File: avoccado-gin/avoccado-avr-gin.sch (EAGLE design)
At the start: 55 parts, among them Q1 16MHz, Q2 FET, U1 MPU-6000QFN-24, U2 MCP73831

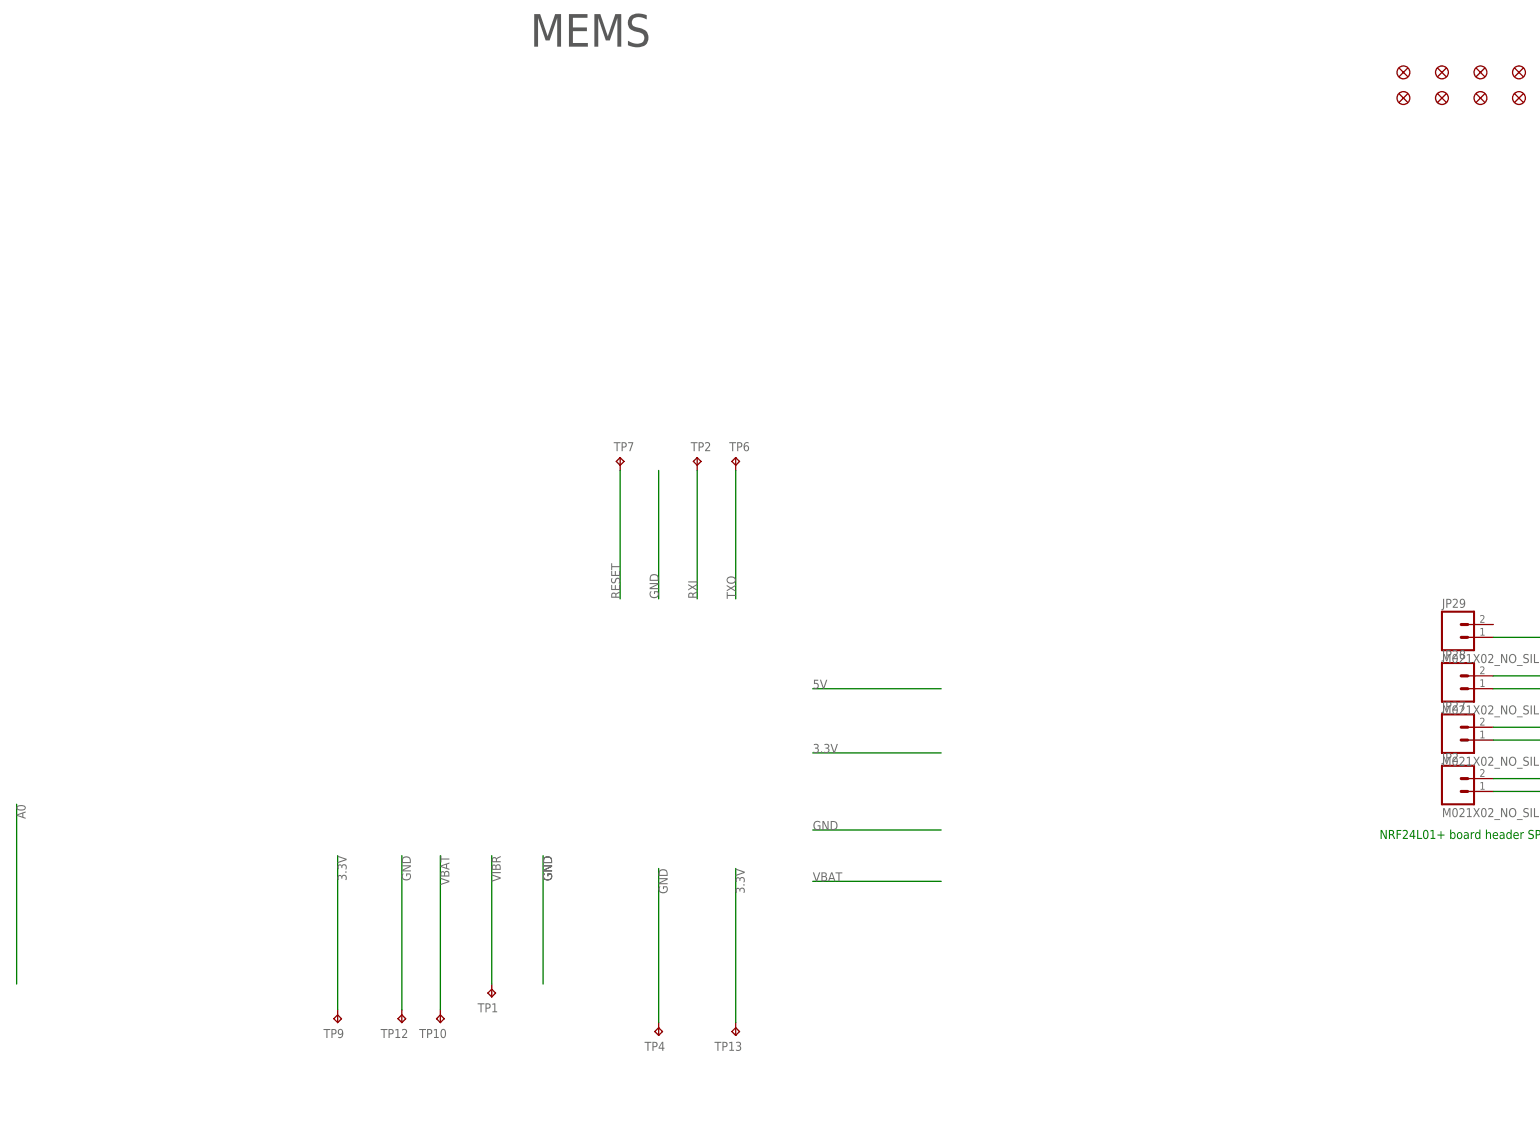
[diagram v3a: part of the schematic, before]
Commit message: add SMD pads to bottom layer
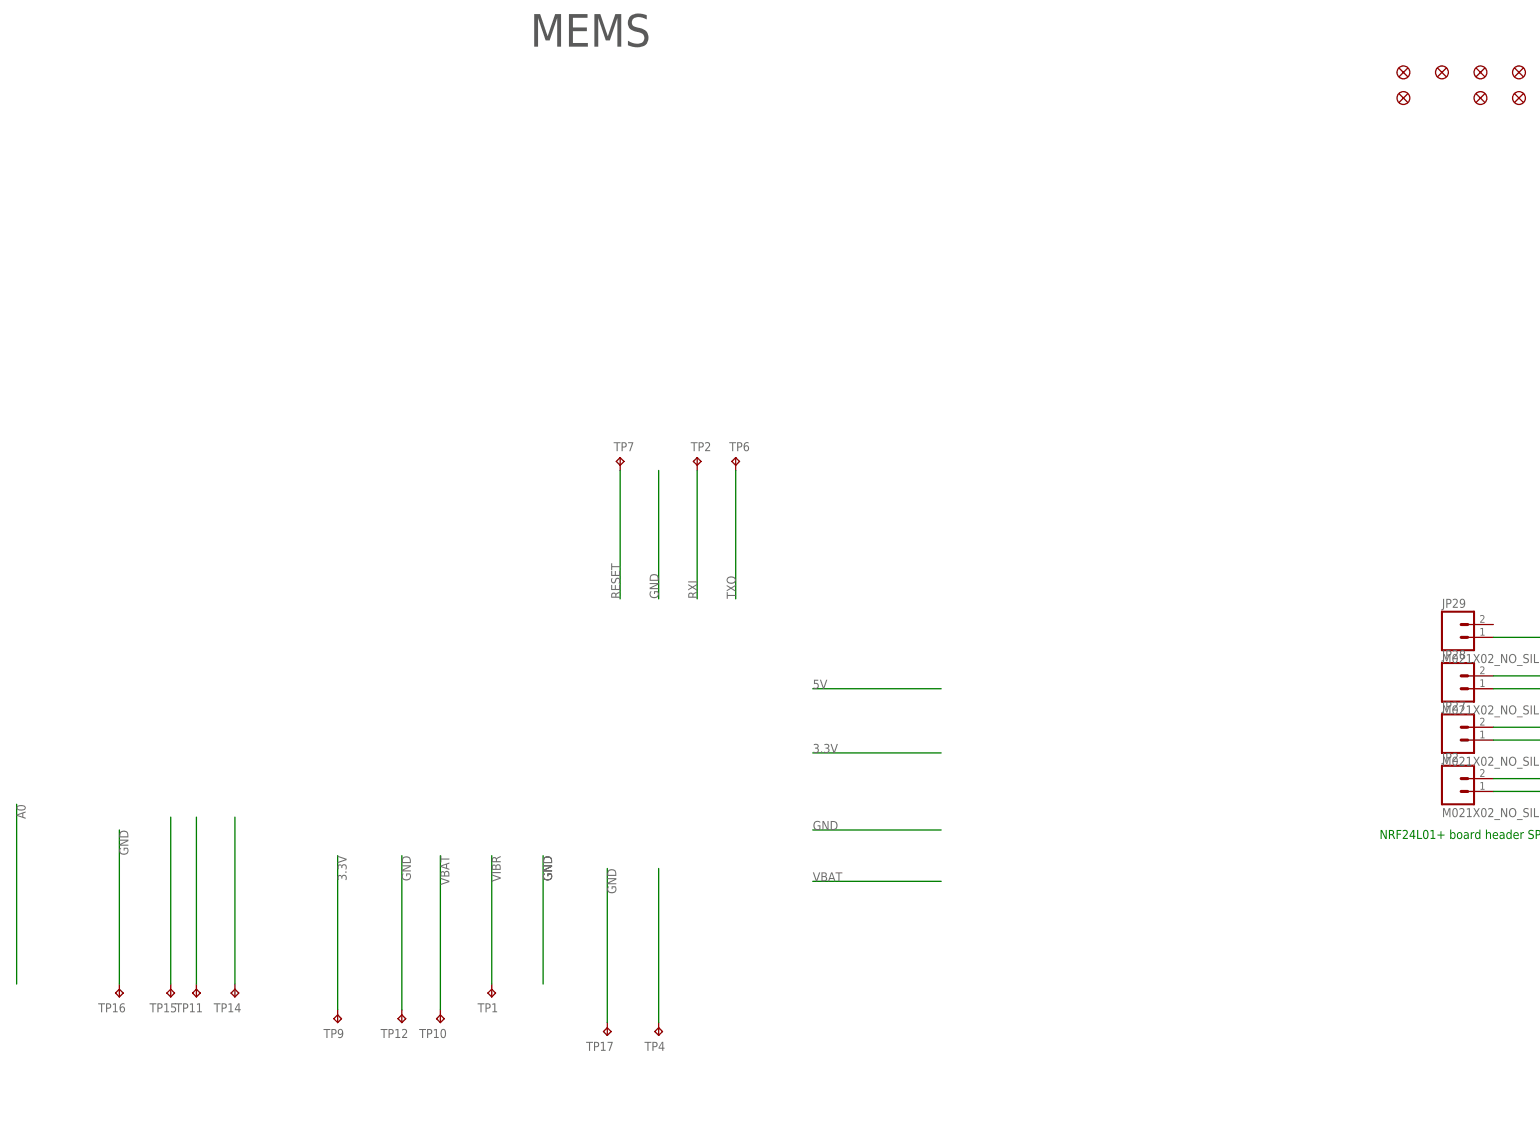
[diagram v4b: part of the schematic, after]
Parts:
- removed FID7: FIDUCIALUFIDUCIAL, SparkFun-Aesthetics:FIDUCIALUFIDUCIAL
- removed TP13: TPTP20R, testpad:TPTP20R
- added TP11, TP14, TP15, TP16, TP17: TPTP20R, testpad:TPTP20R
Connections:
- net 3.3V: no longer TP13.TP
- net D5: now also TP15.TP
- net D7: now also TP14.TP
- net D8: now also TP11.TP
- net GND: now also TP16.TP, TP17.TP; no longer TP4.TP
- net VBAT: now also TP4.TP
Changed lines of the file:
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@@
 <part name="TP10" library="testpad" deviceset="TP" device="TP20R"/>
 <part name="TP12" library="testpad" deviceset="TP" device="TP20R"/>
-<part name="TP13" library="testpad" deviceset="TP" device="TP20R"/>
 <part name="TP4" library="testpad" deviceset="TP" device="TP20R"/>
 <part name="FRAME2" library="frames" deviceset="LETTER_L" device=""/>
@@
 <part name="FID5" library="SparkFun-Aesthetics" deviceset="FIDUCIAL" device="UFIDUCIAL"/>
 <part name="FID6" library="SparkFun-Aesthetics" deviceset="FIDUCIAL" device="UFIDUCIAL"/>
-<part name="FID7" library="SparkFun-Aesthetics" deviceset="FIDUCIAL" device="UFIDUCIAL"/>
 <part name="FID8" library="SparkFun-Aesthetics" deviceset="FIDUCIAL" device="UFIDUCIAL"/>
 <part name="FID9" library="SparkFun-Aesthetics" deviceset="FIDUCIAL" device="UFIDUCIAL"/>
@@
 <part name="TP8" library="testpad" deviceset="TP" device="TP20R"/>
 <part name="TP9" library="testpad" deviceset="TP" device="TP20R"/>
+<part name="TP11" library="testpad" deviceset="TP" device="TP20R"/>
+<part name="TP14" library="testpad" deviceset="TP" device="TP20R"/>
+<part name="TP15" library="testpad" deviceset="TP" device="TP20R"/>
+<part name="TP16" library="testpad" deviceset="TP" device="TP20R"/>
+<part name="TP17" library="testpad" deviceset="TP" device="TP20R"/>
 </parts>
 <sheets>
@@
 <instance part="TP10" gate="G$1" x="421.64" y="58.42" rot="R180"/>
 <instance part="TP12" gate="G$1" x="414.02" y="58.42" rot="R180"/>
-<instance part="TP13" gate="G$1" x="480.06" y="55.88" rot="R180"/>
 <instance part="TP4" gate="G$1" x="464.82" y="55.88" rot="R180"/>
 <instance part="FRAME2" gate="G$1" x="0" y="226.06"/>
@@
 <instance part="FID5" gate="G$1" x="642.62" y="246.38"/>
 <instance part="FID6" gate="G$1" x="612.14" y="241.3"/>
-<instance part="FID7" gate="G$1" x="619.76" y="241.3"/>
 <instance part="FID8" gate="G$1" x="627.38" y="241.3"/>
 <instance part="FID9" gate="G$1" x="635" y="241.3"/>
@@
 <instance part="TP8" gate="G$1" x="330.2" y="63.5" rot="R180"/>
 <instance part="TP9" gate="G$1" x="401.32" y="58.42" rot="R180"/>
+<instance part="TP11" gate="G$1" x="373.38" y="63.5" rot="R180"/>
+<instance part="TP14" gate="G$1" x="381" y="63.5" rot="R180"/>
+<instance part="TP15" gate="G$1" x="368.3" y="63.5" rot="R180"/>
+<instance part="TP16" gate="G$1" x="358.14" y="63.5" rot="R180"/>
+<instance part="TP17" gate="G$1" x="454.66" y="55.88" rot="R180"/>
 </instances>
 <busses>
@@
 </segment>
 <segment>
-<wire x1="464.82" y1="58.42" x2="464.82" y2="88.9" width="0.1524" layer="91"/>
-<pinref part="TP4" gate="G$1" pin="TP"/>
-<label x="464.82" y="88.9" size="1.778" layer="95" rot="R270"/>
-</segment>
-<segment>
 <pinref part="JP22" gate="G$1" pin="SHIELD"/>
 <pinref part="GND16" gate="1" pin="GND"/>
@@
 <pinref part="C2" gate="G$1" pin="1"/>
 <pinref part="GND17" gate="1" pin="GND"/>
+</segment>
+<segment>
+<wire x1="358.14" y1="66.04" x2="358.14" y2="96.52" width="0.1524" layer="91"/>
+<pinref part="TP16" gate="G$1" pin="TP"/>
+<label x="358.14" y="96.52" size="1.778" layer="95" rot="R270"/>
+</segment>
+<segment>
+<wire x1="454.66" y1="58.42" x2="454.66" y2="88.9" width="0.1524" layer="91"/>
+<pinref part="TP17" gate="G$1" pin="TP"/>
+<label x="454.66" y="88.9" size="1.778" layer="95" rot="R270"/>
 </segment>
 </net>
@@
 </segment>
 <segment>
-<wire x1="480.06" y1="88.9" x2="480.06" y2="58.42" width="0.1524" layer="91"/>
-<pinref part="TP13" gate="G$1" pin="TP"/>
-<label x="480.06" y="88.9" size="1.778" layer="95" rot="R270"/>
-</segment>
-<segment>
 <pinref part="C2" gate="G$1" pin="2"/>
 <pinref part="P+5" gate="G$1" pin="3.3V"/>
@@
 <label x="218.44" y="109.22" size="1.778" layer="95"/>
 <pinref part="U3" gate="U$1" pin="PB0(ICP)"/>
+</segment>
+<segment>
+<wire x1="373.38" y1="66.04" x2="373.38" y2="99.06" width="0.1524" layer="91"/>
+<pinref part="TP11" gate="G$1" pin="TP"/>
 </segment>
 </net>
@@
 <pinref part="U3" gate="U$1" pin="PD5(T1)"/>
 </segment>
+<segment>
+<wire x1="368.3" y1="66.04" x2="368.3" y2="99.06" width="0.1524" layer="91"/>
+<pinref part="TP15" gate="G$1" pin="TP"/>
+</segment>
 </net>
 <net name="D6" class="0">
@@
 <label x="218.44" y="114.3" size="1.778" layer="95"/>
 <pinref part="U3" gate="U$1" pin="PD7(AIN1)"/>
+</segment>
+<segment>
+<wire x1="381" y1="66.04" x2="381" y2="99.06" width="0.1524" layer="91"/>
+<pinref part="TP14" gate="G$1" pin="TP"/>
 </segment>
 </net>
@@
 <label x="421.64" y="91.44" size="1.778" layer="95" rot="R270"/>
 </segment>
-</net>
+<segment>
+<wire x1="464.82" y1="58.42" x2="464.82" y2="88.9" width="0.1524" layer="91"/>
+<pinref part="TP4" gate="G$1" pin="TP"/>
+</segment>
+</net>

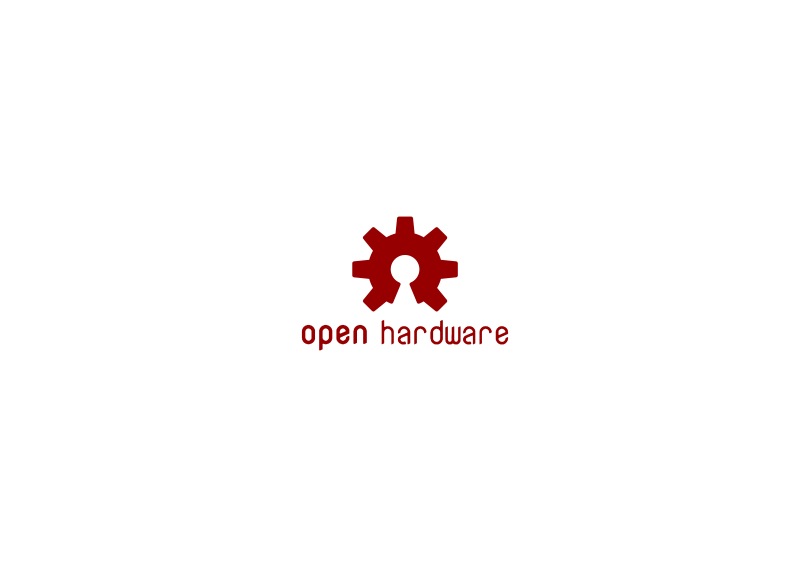
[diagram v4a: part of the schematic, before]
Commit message: Finish silkscreen with a wide A° instead of pin declarations
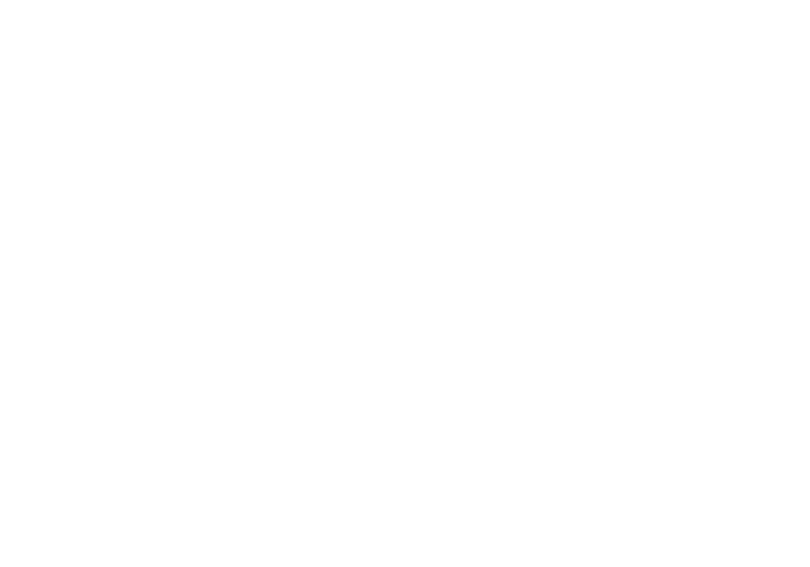
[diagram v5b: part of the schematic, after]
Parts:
- removed LOGO1: OSHW-LOGOS, SparkFun-Aesthetics:OSHW-LOGOS
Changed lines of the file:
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@@
 <part name="FRAME6" library="frames" deviceset="LETTER_L" device=""/>
 <part name="FID2" library="SparkFun-Aesthetics" deviceset="FIDUCIAL" device="UFIDUCIAL"/>
-<part name="LOGO1" library="SparkFun-Aesthetics" deviceset="OSHW-LOGO" device="S"/>
 <part name="FID1" library="SparkFun-Aesthetics" deviceset="FIDUCIAL" device="UFIDUCIAL"/>
 <part name="FID3" library="SparkFun-Aesthetics" deviceset="FIDUCIAL" device="UFIDUCIAL"/>
@@
 <instance part="FRAME6" gate="G$2" x="721.36" y="0"/>
 <instance part="FID2" gate="G$1" x="612.14" y="246.38"/>
-<instance part="LOGO1" gate="G$1" x="800.1" y="276.86"/>
 <instance part="FID1" gate="G$1" x="619.76" y="246.38"/>
 <instance part="FID3" gate="G$1" x="627.38" y="246.38"/>

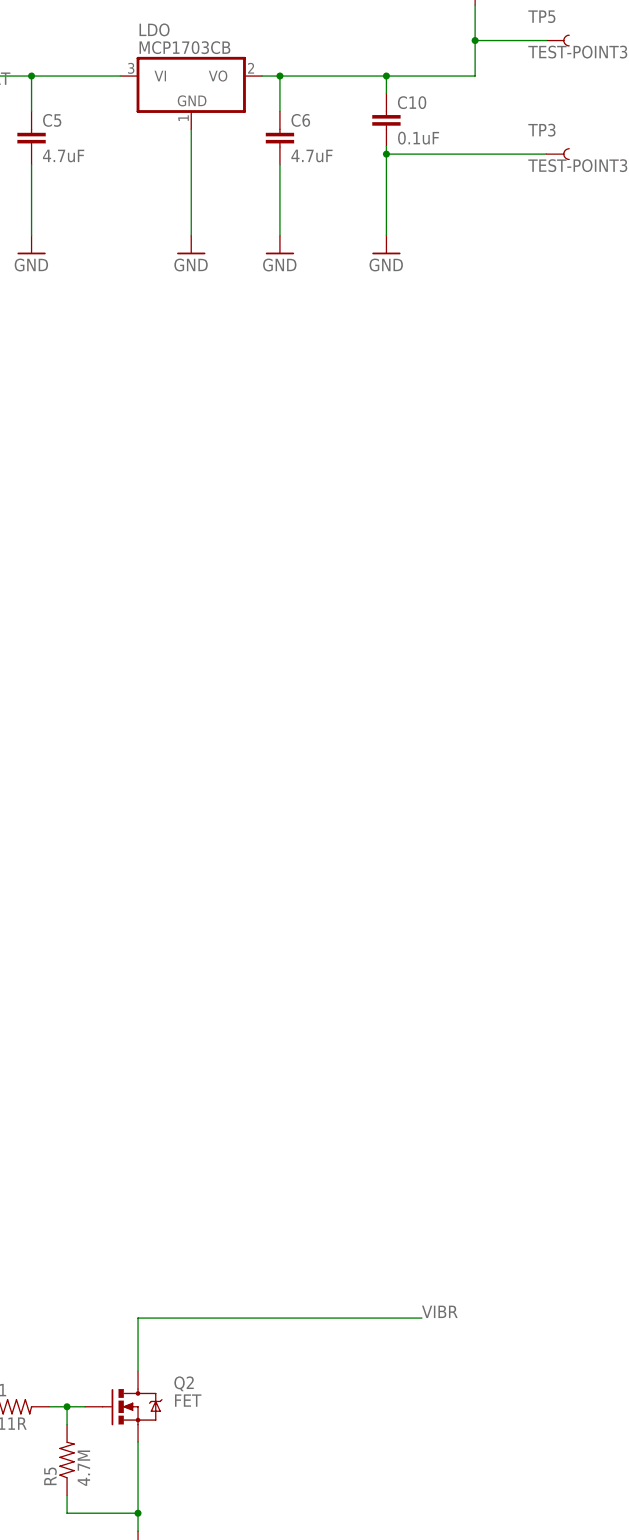
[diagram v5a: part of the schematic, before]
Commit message: render PNG preview
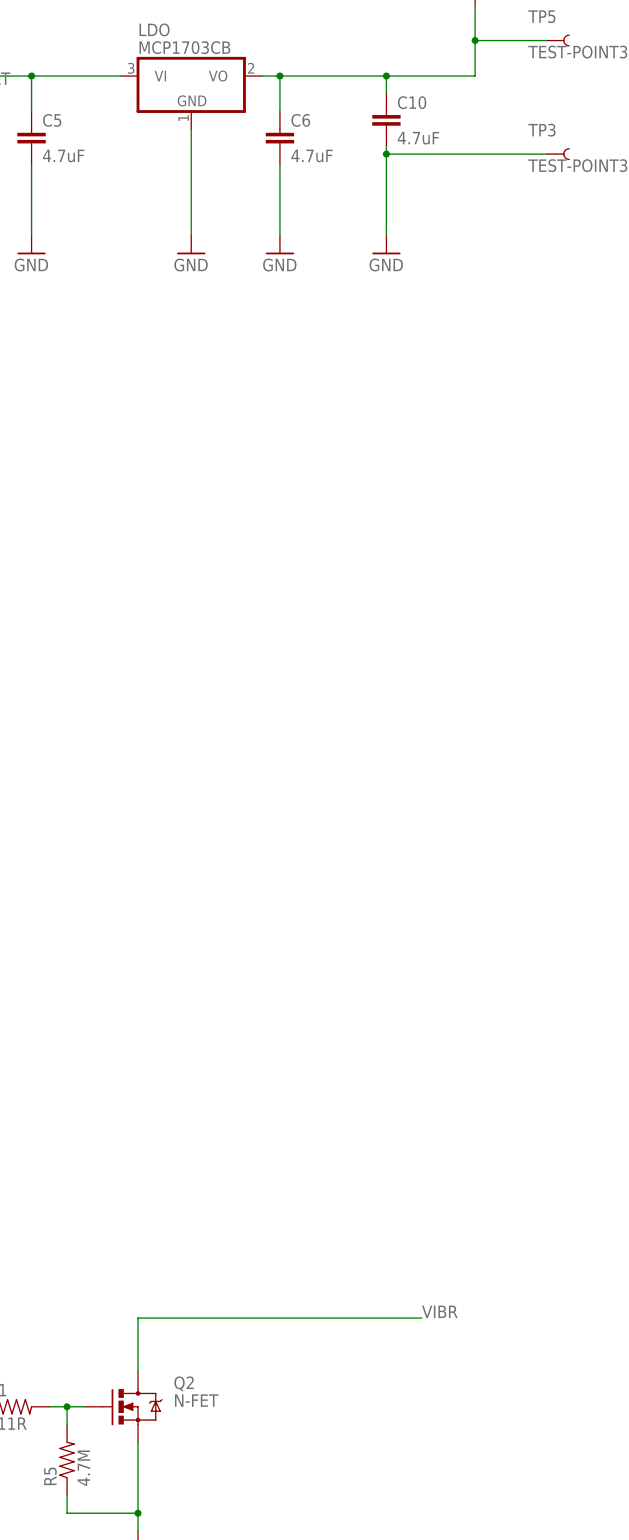
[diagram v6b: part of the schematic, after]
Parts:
- C10: value 0.1uF -> 4.7uF
- Q2: value FET -> N-FET
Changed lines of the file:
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@@
 </classes>
 <parts>
-<part name="C10" library="rcl" deviceset="C-EU" device="C0603" value="0.1uF"/>
+<part name="C10" library="rcl" deviceset="C-EU" device="C0603" value="4.7uF"/>
 <part name="FRAME1" library="SparkFun" deviceset="FRAME-LETTER" device=""/>
 <part name="GND25" library="SparkFun" deviceset="GND" device=""/>
@@
 <part name="P+1" library="SparkFun" deviceset="3.3V" device="" value="3V3"/>
 <part name="GND5" library="SparkFun" deviceset="GND" device=""/>
-<part name="Q2" library="SparkFun-DiscreteSemi" deviceset="MOSFET-NCHANNEL" device="BSS123LT1G" value="FET"/>
+<part name="Q2" library="SparkFun-DiscreteSemi" deviceset="MOSFET-NCHANNEL" device="BSS123LT1G" value="N-FET"/>
 <part name="R1" library="SparkFun-Resistors" deviceset="RESISTOR" device="0603" value="511R"/>
 <part name="LDO" library="linear" deviceset="MCP1703" device="CB"/>

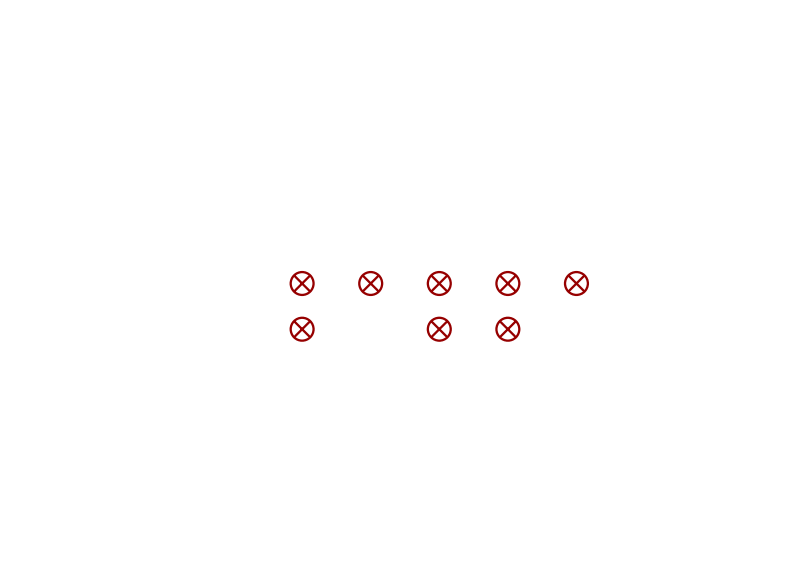
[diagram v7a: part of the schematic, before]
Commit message: add PCBs with ICSP adapters and panelize
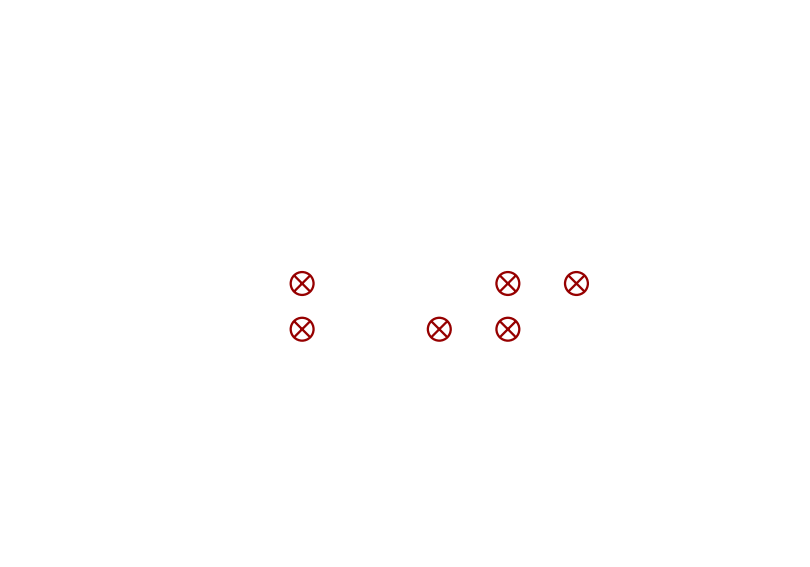
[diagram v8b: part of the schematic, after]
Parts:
- removed FID1, FID3: FIDUCIALUFIDUCIAL, SparkFun-Aesthetics:FIDUCIALUFIDUCIAL
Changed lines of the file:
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@@
 <part name="FRAME6" library="frames" deviceset="LETTER_L" device=""/>
 <part name="FID2" library="SparkFun-Aesthetics" deviceset="FIDUCIAL" device="UFIDUCIAL"/>
-<part name="FID1" library="SparkFun-Aesthetics" deviceset="FIDUCIAL" device="UFIDUCIAL"/>
-<part name="FID3" library="SparkFun-Aesthetics" deviceset="FIDUCIAL" device="UFIDUCIAL"/>
 <part name="JP22" library="SparkFun-Connectors" deviceset="USB_MICROB_PLUG" device="CONN-11752"/>
 <part name="GND16" library="SparkFun" deviceset="GND" device=""/>
@@
 <instance part="FRAME6" gate="G$2" x="721.36" y="0"/>
 <instance part="FID2" gate="G$1" x="612.14" y="246.38"/>
-<instance part="FID1" gate="G$1" x="619.76" y="246.38"/>
-<instance part="FID3" gate="G$1" x="627.38" y="246.38"/>
 <instance part="JP22" gate="G$1" x="55.88" y="360.68" rot="R180"/>
 <instance part="GND16" gate="1" x="43.18" y="353.06"/>
